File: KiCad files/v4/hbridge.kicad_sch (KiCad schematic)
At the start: 2 parts

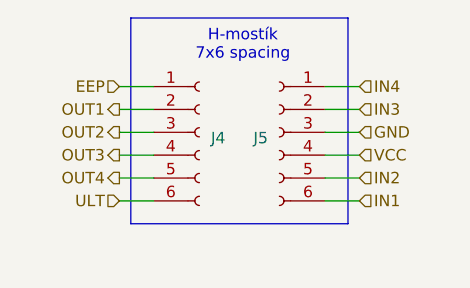
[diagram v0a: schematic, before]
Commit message: Generated output files for docs. Removed old fabrication files.
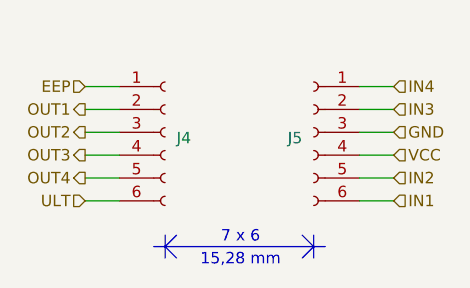
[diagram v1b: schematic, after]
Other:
- note added: "15,28 mm"
- note added: "7 x 6"
- note removed: "H-mostík 7x6 spacing"
- moved on the sheet: J4, J5
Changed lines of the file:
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@@
 		(comment 1 "H-bridge pin socket")
 	)
-	(rectangle
-		(start 134.62 86.36)
-		(end 158.75 109.22)
-		(stroke
-			(width 0)
-			(type default)
-		)
-		(fill
-			(type none)
-		)
-	)
-	(text "H-mostík\n7x6 spacing"
+	(text "15,28 mm"
 		(exclude_from_sim no)
-		(at 147.066 89.408 0)
-		(effects
-			(font
-				(size 1.27 1.27)
-			)
-		)
-	)
-	(wire
-		(pts
-			(xy 133.35 99.06) (xy 137.16 99.06)
-		)
-		(stroke
-			(width 0)
-			(type default)
-		)
-	)
-	(wire
-		(pts
-			(xy 133.35 106.68) (xy 137.16 106.68)
-		)
-		(stroke
-			(width 0)
-			(type default)
-		)
-	)
-	(wire
-		(pts
-			(xy 156.21 96.52) (xy 160.02 96.52)
-		)
-		(stroke
-			(width 0)
-			(type default)
-		)
-	)
-	(wire
-		(pts
-			(xy 156.21 104.14) (xy 160.02 104.14)
-		)
-		(stroke
-			(width 0)
-			(type default)
-		)
-	)
-	(wire
-		(pts
-			(xy 133.35 96.52) (xy 137.16 96.52)
-		)
-		(stroke
-			(width 0)
-			(type default)
-		)
-	)
-	(wire
-		(pts
-			(xy 156.21 106.68) (xy 160.02 106.68)
-		)
-		(stroke
-			(width 0)
-			(type default)
-		)
-	)
-	(wire
-		(pts
-			(xy 133.35 93.98) (xy 137.16 93.98)
-		)
-		(stroke
-			(width 0)
-			(type default)
-		)
-	)
-	(wire
-		(pts
-			(xy 156.21 99.06) (xy 160.02 99.06)
-		)
-		(stroke
-			(width 0)
-			(type default)
-		)
-	)
-	(wire
-		(pts
-			(xy 133.35 101.6) (xy 137.16 101.6)
-		)
-		(stroke
-			(width 0)
-			(type default)
-		)
-	)
-	(wire
-		(pts
-			(xy 156.21 93.98) (xy 160.02 93.98)
-		)
-		(stroke
-			(width 0)
-			(type default)
-		)
-	)
-	(wire
-		(pts
-			(xy 133.35 104.14) (xy 137.16 104.14)
-		)
-		(stroke
-			(width 0)
-			(type default)
-		)
-	)
-	(wire
-		(pts
-			(xy 156.21 101.6) (xy 160.02 101.6)
+		(at 146.812 113.284 0)
+		(effects
+			(font
+				(size 1.27 1.27)
+			)
+		)
+	)
+	(text "7 x 6"
+		(exclude_from_sim no)
+		(at 146.812 110.744 0)
+		(effects
+			(font
+				(size 1.27 1.27)
+			)
+		)
+	)
+	(polyline
+		(pts
+			(xy 138.43 110.49) (xy 138.43 113.03)
+		)
+		(stroke
+			(width 0)
+			(type default)
+		)
+	)
+	(wire
+		(pts
+			(xy 129.54 99.06) (xy 133.35 99.06)
+		)
+		(stroke
+			(width 0)
+			(type default)
+		)
+	)
+	(wire
+		(pts
+			(xy 129.54 106.68) (xy 133.35 106.68)
+		)
+		(stroke
+			(width 0)
+			(type default)
+		)
+	)
+	(wire
+		(pts
+			(xy 160.02 96.52) (xy 163.83 96.52)
+		)
+		(stroke
+			(width 0)
+			(type default)
+		)
+	)
+	(polyline
+		(pts
+			(xy 138.43 111.76) (xy 139.7 113.03)
+		)
+		(stroke
+			(width 0)
+			(type default)
+		)
+	)
+	(wire
+		(pts
+			(xy 160.02 104.14) (xy 163.83 104.14)
+		)
+		(stroke
+			(width 0)
+			(type default)
+		)
+	)
+	(polyline
+		(pts
+			(xy 153.67 113.03) (xy 154.94 111.76)
+		)
+		(stroke
+			(width 0)
+			(type default)
+		)
+	)
+	(polyline
+		(pts
+			(xy 137.16 111.76) (xy 156.21 111.76)
+		)
+		(stroke
+			(width 0)
+			(type default)
+		)
+	)
+	(wire
+		(pts
+			(xy 129.54 96.52) (xy 133.35 96.52)
+		)
+		(stroke
+			(width 0)
+			(type default)
+		)
+	)
+	(polyline
+		(pts
+			(xy 154.94 110.49) (xy 154.94 113.03)
+		)
+		(stroke
+			(width 0)
+			(type default)
+		)
+	)
+	(wire
+		(pts
+			(xy 160.02 106.68) (xy 163.83 106.68)
+		)
+		(stroke
+			(width 0)
+			(type default)
+		)
+	)
+	(polyline
+		(pts
+			(xy 153.67 110.49) (xy 154.94 111.76)
+		)
+		(stroke
+			(width 0)
+			(type default)
+		)
+	)
+	(wire
+		(pts
+			(xy 129.54 93.98) (xy 133.35 93.98)
+		)
+		(stroke
+			(width 0)
+			(type default)
+		)
+	)
+	(wire
+		(pts
+			(xy 160.02 99.06) (xy 163.83 99.06)
+		)
+		(stroke
+			(width 0)
+			(type default)
+		)
+	)
+	(wire
+		(pts
+			(xy 129.54 101.6) (xy 133.35 101.6)
+		)
+		(stroke
+			(width 0)
+			(type default)
+		)
+	)
+	(wire
+		(pts
+			(xy 160.02 93.98) (xy 163.83 93.98)
+		)
+		(stroke
+			(width 0)
+			(type default)
+		)
+	)
+	(wire
+		(pts
+			(xy 129.54 104.14) (xy 133.35 104.14)
+		)
+		(stroke
+			(width 0)
+			(type default)
+		)
+	)
+	(polyline
+		(pts
+			(xy 138.43 111.76) (xy 139.7 110.49)
+		)
+		(stroke
+			(width 0)
+			(type default)
+		)
+	)
+	(wire
+		(pts
+			(xy 160.02 101.6) (xy 163.83 101.6)
 		)
 		(stroke
@@
 	(hierarchical_label "EEP"
 		(shape input)
-		(at 133.35 93.98 180)
+		(at 129.54 93.98 180)
 		(effects
 			(font
@@
 	(hierarchical_label "ULT"
 		(shape input)
-		(at 133.35 106.68 180)
+		(at 129.54 106.68 180)
 		(effects
 			(font
@@
 	(hierarchical_label "GND"
 		(shape input)
-		(at 160.02 99.06 0)
+		(at 163.83 99.06 0)
 		(effects
 			(font
@@
 	(hierarchical_label "IN2"
 		(shape input)
-		(at 160.02 104.14 0)
+		(at 163.83 104.14 0)
 		(effects
 			(font
@@
 	(hierarchical_label "IN1"
 		(shape input)
-		(at 160.02 106.68 0)
+		(at 163.83 106.68 0)
 		(effects
 			(font
@@
 	(hierarchical_label "VCC"
 		(shape input)
-		(at 160.02 101.6 0)
+		(at 163.83 101.6 0)
 		(effects
 			(font
@@
 	(hierarchical_label "IN3"
 		(shape input)
-		(at 160.02 96.52 0)
+		(at 163.83 96.52 0)
 		(effects
 			(font
@@
 	(hierarchical_label "OUT3"
 		(shape output)
-		(at 133.35 101.6 180)
+		(at 129.54 101.6 180)
 		(effects
 			(font
@@
 	(hierarchical_label "OUT2"
 		(shape output)
-		(at 133.35 99.06 180)
+		(at 129.54 99.06 180)
 		(effects
 			(font
@@
 	(hierarchical_label "OUT4"
 		(shape output)
-		(at 133.35 104.14 180)
+		(at 129.54 104.14 180)
 		(effects
 			(font
@@
 	(hierarchical_label "IN4"
 		(shape input)
-		(at 160.02 93.98 0)
+		(at 163.83 93.98 0)
 		(effects
 			(font
@@
 	(hierarchical_label "OUT1"
 		(shape output)
-		(at 133.35 96.52 180)
+		(at 129.54 96.52 180)
 		(effects
 			(font
@@
 	(symbol
 		(lib_id "Connector:Conn_01x06_Socket")
-		(at 142.24 99.06 0)
+		(at 138.43 99.06 0)
 		(unit 1)
 		(exclude_from_sim no)
@@
 		(dnp no)
 		(property "Reference" "J4"
-			(at 143.51 99.6949 0)
+			(at 139.7 99.6949 0)
 			(effects
 				(font
@@
 		)
 		(property "Value" "~"
-			(at 143.51 101.6 0)
+			(at 139.7 101.6 0)
 			(effects
 				(font
@@
 		)
 		(property "Footprint" "Connector_PinSocket_2.54mm:PinSocket_1x06_P2.54mm_Vertical"
-			(at 142.24 99.06 0)
+			(at 138.43 99.06 0)
 			(effects
 				(font
@@
 		)
 		(property "Datasheet" "~"
-			(at 142.24 99.06 0)
+			(at 138.43 99.06 0)
 			(effects
 				(font
@@
 		)
 		(property "Description" "Generic connector, single row, 01x06, script generated"
-			(at 142.24 99.06 0)
+			(at 138.43 99.06 0)
 			(effects
 				(font
@@
 	(symbol
 		(lib_id "Connector:Conn_01x06_Socket")
-		(at 151.13 99.06 0)
+		(at 154.94 99.06 0)
 		(mirror y)
 		(unit 1)
@@
 		(dnp no)
 		(property "Reference" "J5"
-			(at 149.86 99.6949 0)
+			(at 153.67 99.6949 0)
 			(effects
 				(font
@@
 		)
 		(property "Value" "~"
-			(at 149.86 101.6 0)
+			(at 153.67 101.6 0)
 			(effects
 				(font
@@
 		)
 		(property "Footprint" "Connector_PinSocket_2.54mm:PinSocket_1x06_P2.54mm_Vertical"
-			(at 151.13 99.06 0)
+			(at 154.94 99.06 0)
 			(effects
 				(font
@@
 		)
 		(property "Datasheet" "~"
-			(at 151.13 99.06 0)
+			(at 154.94 99.06 0)
 			(effects
 				(font
@@
 		)
 		(property "Description" "Generic connector, single row, 01x06, script generated"
-			(at 151.13 99.06 0)
-			(effects
-				(font
+			(at 154.94 99.06 0)
+			(effects
+				(font
